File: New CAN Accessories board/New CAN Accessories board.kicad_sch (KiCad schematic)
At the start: 22 parts, among them J10 39301040, J11 ATF13-2P-BM03, J12 Conn_01x02_Pin, J9 39301060, T1 MCP2562FD-E_SN, U1 NUCLEO_L432KC

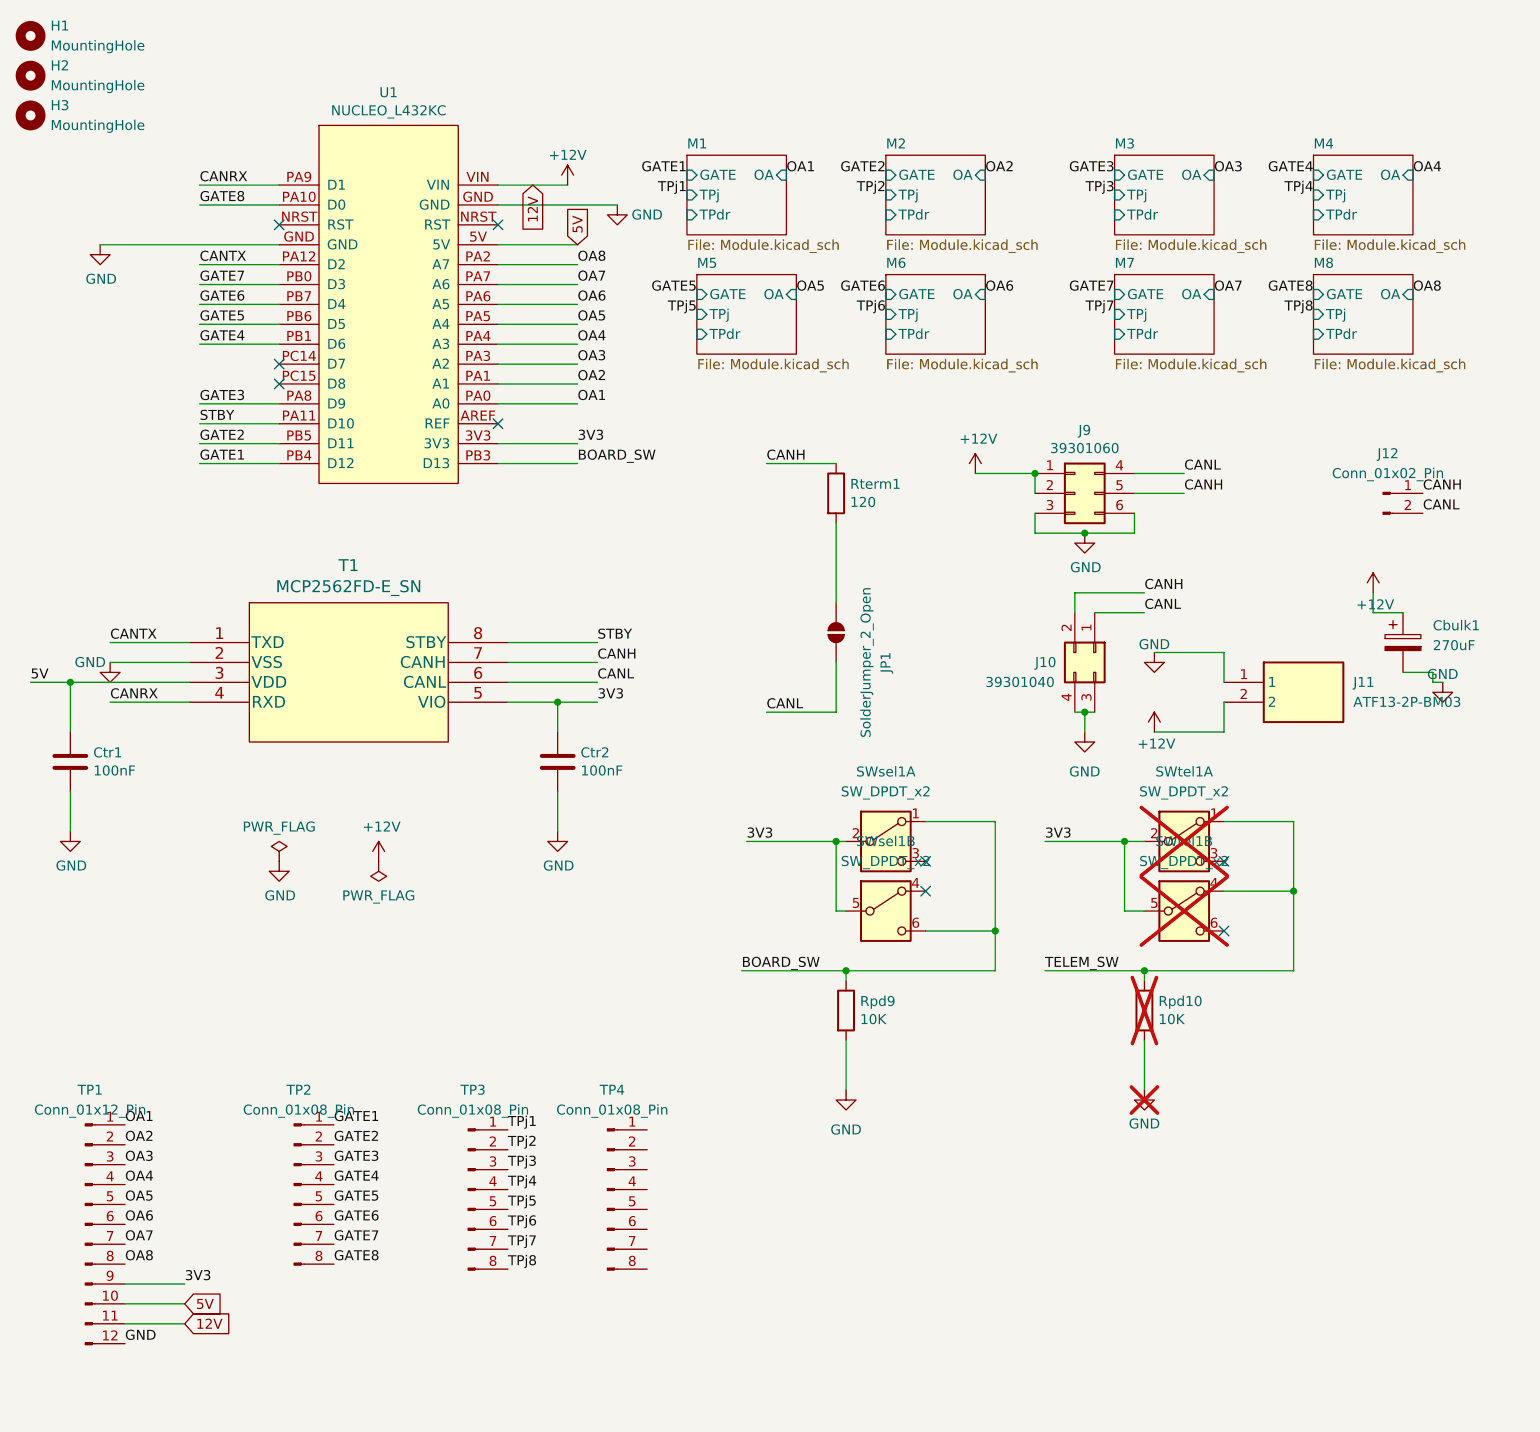
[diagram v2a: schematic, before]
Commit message: 1x16 header test points
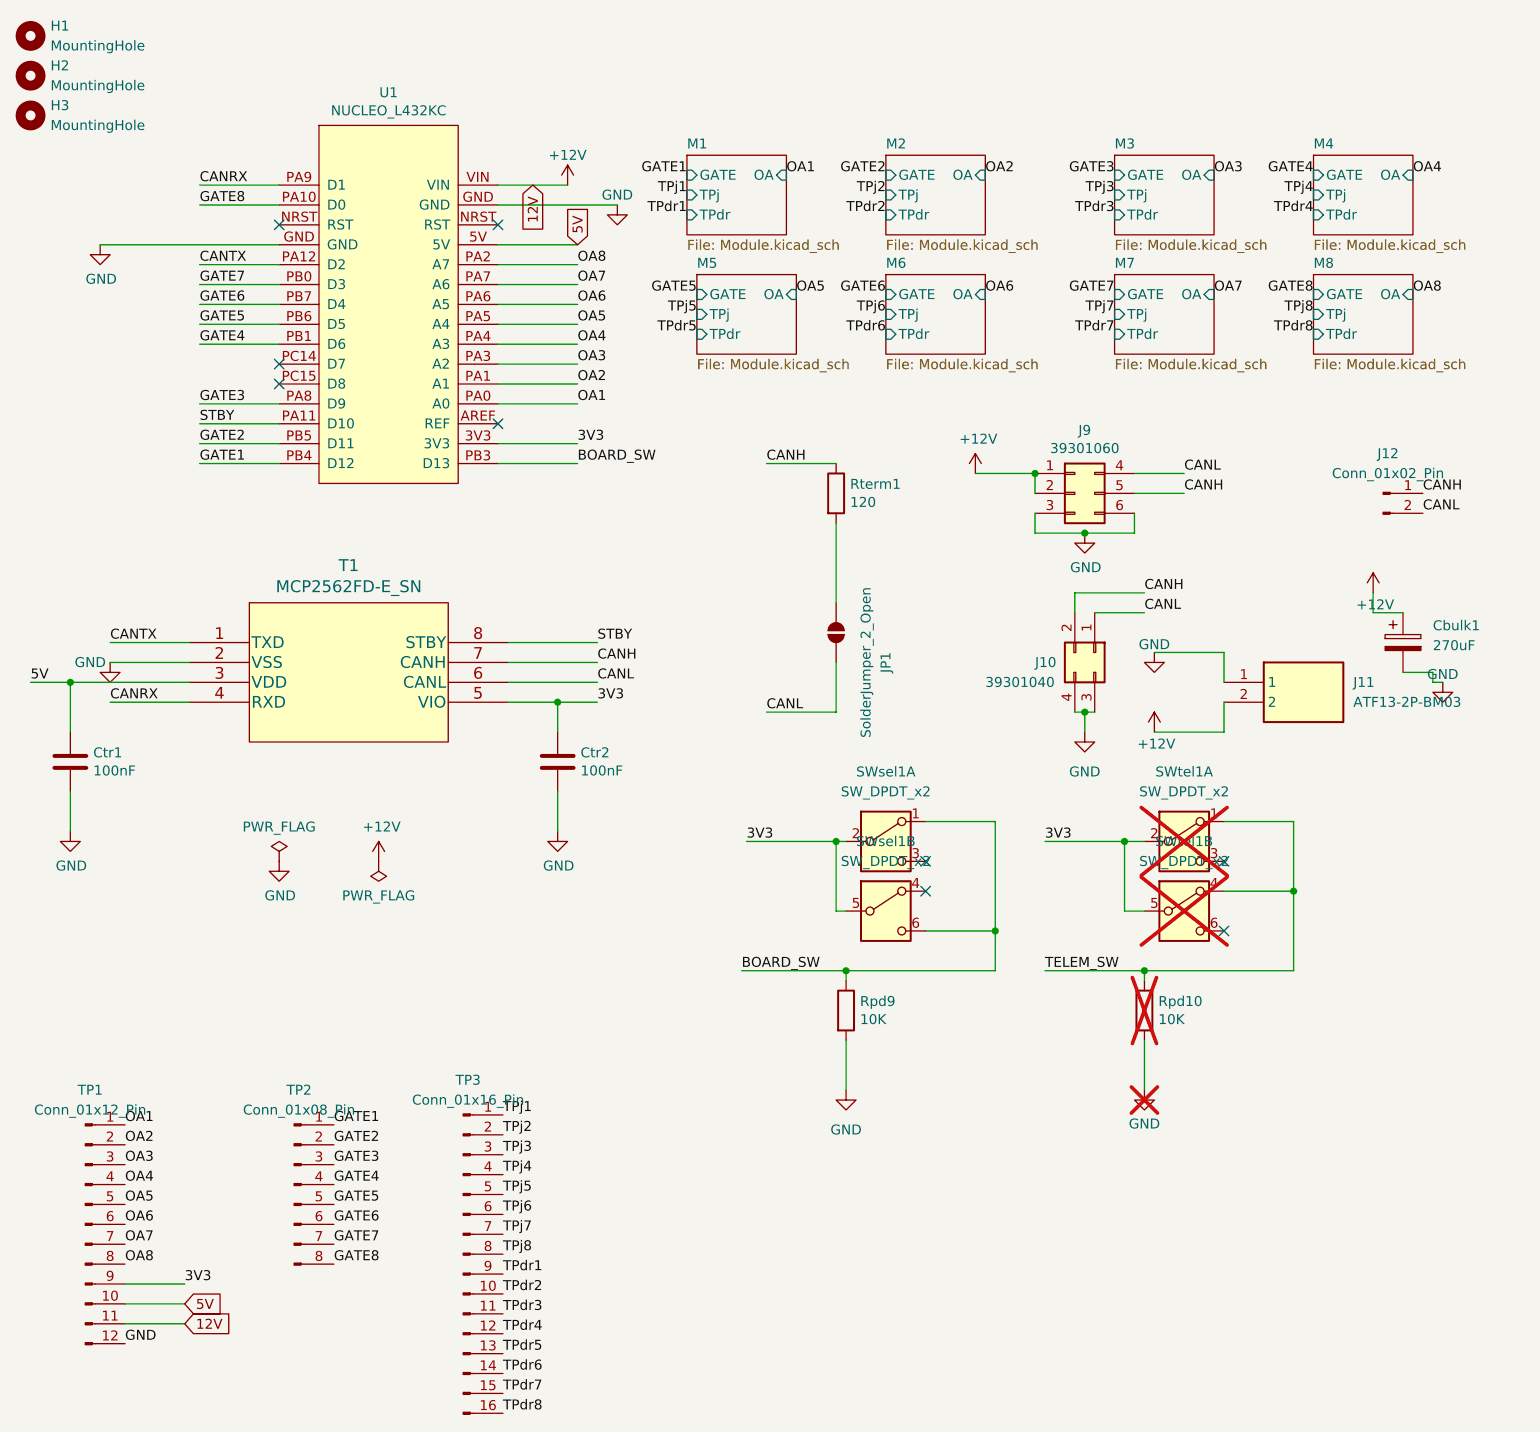
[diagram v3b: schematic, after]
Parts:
- removed TP3, TP4: Conn_01x08_Pin, Connector_PinHeader_2.54mm:PinHeader_1x08_P2.54mm_Vertical, symbol Connector:Conn_01x08_Pin
- added TP3: Conn_01x16_Pin, Connector_PinHeader_2.54mm:PinHeader_1x16_P2.54mm_Vertical, symbol Connector:Conn_01x16_Pin
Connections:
- net TPj1: now also TP3.1 (Pin_1)
- net TPj2: now also TP3.2 (Pin_2)
- net TPj3: now also TP3.3 (Pin_3)
- net TPj4: now also TP3.4 (Pin_4)
- net TPj5: now also TP3.5 (Pin_5)
- net TPj6: now also TP3.6 (Pin_6)
- net TPj7: now also TP3.7 (Pin_7)
- net TPj8: now also TP3.8 (Pin_8)
- new net TPdr1: TP3.9 (Pin_9)
- new net TPdr2: TP3.10 (Pin_10)
- new net TPdr3: TP3.11 (Pin_11)
- new net TPdr4: TP3.12 (Pin_12)
- new net TPdr5: TP3.13 (Pin_13)
- new net TPdr6: TP3.14 (Pin_14)
- new net TPdr7: TP3.15 (Pin_15)
- new net TPdr8: TP3.16 (Pin_16)

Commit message: finalized PCB design
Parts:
- removed J12: Conn_01x02_Pin, Connector_PinHeader_2.54mm:PinHeader_1x02_P2.54mm_Vertical, symbol Connector:Conn_01x02_Pin
- added J12: Conn_01x03_Pin, Connector_PinHeader_2.54mm:PinHeader_1x03_P2.54mm_Vertical, symbol Connector:Conn_01x03_Pin
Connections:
- net CANH: now also J12.1 (Pin_1)
- net CANL: now also J12.2 (Pin_2)
- net GND: now also J12.3 (Pin_3)
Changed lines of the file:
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@@
 	(wire
 		(pts
+			(xy 203.2 85.09) (xy 207.01 85.09)
+		)
+		(stroke
+			(width 0)
+			(type default)
+		)
+	)
+	(wire
+		(pts
 			(xy 186.69 130.81) (xy 186.69 140.97)
 		)
@@
 	)
 	(symbol
+		(lib_id "Connector:Conn_01x03_Pin")
+		(at 198.12 82.55 0)
+		(unit 1)
+		(exclude_from_sim no)
+		(in_bom yes)
+		(on_board yes)
+		(dnp no)
+		(fields_autoplaced yes)
+		(property "Reference" "J12"
+			(at 198.755 74.93 0)
+			(effects
+				(font
+					(size 1.27 1.27)
+				)
+			)
+		)
+		(property "Value" "Conn_01x03_Pin"
+			(at 198.755 77.47 0)
+			(effects
+				(font
+					(size 1.27 1.27)
+				)
+			)
+		)
+		(property "Footprint" "Connector_PinHeader_2.54mm:PinHeader_1x03_P2.54mm_Vertical"
+			(at 198.12 82.55 0)
+			(effects
+				(font
+					(size 1.27 1.27)
+				)
+				(hide yes)
+			)
+		)
+		(property "Datasheet" "~"
+			(at 198.12 82.55 0)
+			(effects
+				(font
+					(size 1.27 1.27)
+				)
+				(hide yes)
+			)
+		)
+		(property "Description" "Generic connector, single row, 01x03, script generated"
+			(at 198.12 82.55 0)
+			(effects
+				(font
+					(size 1.27 1.27)
+				)
+				(hide yes)
+			)
+		)
+		(pin "2"
+		)
+		(pin "3"
+		)
+		(pin "1"
+		)
+		(instances
+			(project ""
+				(path "/88340f43-3f46-45a6-9393-130e00dc3071"
+					(reference "J12")
+					(unit 1)
+				)
+			)
+		)
+	)
+	(symbol
 		(lib_id "Switch:SW_DPDT_x2")
 		(at 134.62 133.35 0)
@@
 	)
 	(symbol
+		(lib_id "power:GND")
+		(at 207.01 85.09 0)
+		(unit 1)
+		(exclude_from_sim no)
+		(in_bom yes)
+		(on_board yes)
+		(dnp no)
+		(fields_autoplaced yes)
+		(property "Reference" "#PWR039"
+			(at 207.01 91.44 0)
+			(effects
+				(font
+					(size 1.27 1.27)
+				)
+				(hide yes)
+			)
+		)
+		(property "Value" "GND"
+			(at 207.01 90.17 0)
+			(effects
+				(font
+					(size 1.27 1.27)
+				)
+			)
+		)
+		(property "Footprint" ""
+			(at 207.01 85.09 0)
+			(effects
+				(font
+					(size 1.27 1.27)
+				)
+				(hide yes)
+			)
+		)
+		(property "Datasheet" ""
+			(at 207.01 85.09 0)
+			(effects
+				(font
+					(size 1.27 1.27)
+				)
+				(hide yes)
+			)
+		)
+		(property "Description" "Power symbol creates a global label with name \"GND\" , ground"
+			(at 207.01 85.09 0)
+			(effects
+				(font
+					(size 1.27 1.27)
+				)
+				(hide yes)
+			)
+		)
+		(pin "1"
+		)
+		(instances
+			(project ""
+				(path "/88340f43-3f46-45a6-9393-130e00dc3071"
+					(reference "#PWR039")
+					(unit 1)
+				)
+			)
+		)
+	)
+	(symbol
 		(lib_id "Switch:SW_DPDT_x2")
 		(at 172.72 133.35 0)
@@
 					(unit 1)
 				)
-			)
-		)
-	)
-	(symbol
-		(lib_id "Connector:Conn_01x02_Pin")
-		(at 198.12 80.01 0)
-		(unit 1)
-		(exclude_from_sim no)
-		(in_bom yes)
-		(on_board yes)
-		(dnp no)
-		(fields_autoplaced yes)
-		(property "Reference" "J12"
-			(at 198.755 74.93 0)
-			(effects
-				(font
-					(size 1.27 1.27)
-				)
-			)
-		)
-		(property "Value" "Conn_01x02_Pin"
-			(at 198.755 77.47 0)
-			(effects
-				(font
-					(size 1.27 1.27)
-				)
-			)
-		)
-		(property "Footprint" "Connector_PinHeader_2.54mm:PinHeader_1x02_P2.54mm_Vertical"
-			(at 198.12 80.01 0)
-			(effects
-				(font
-					(size 1.27 1.27)
-				)
-				(hide yes)
-			)
-		)
-		(property "Datasheet" "~"
-			(at 198.12 80.01 0)
-			(effects
-				(font
-					(size 1.27 1.27)
-				)
-				(hide yes)
-			)
-		)
-		(property "Description" "Generic connector, single row, 01x02, script generated"
-			(at 198.12 80.01 0)
-			(effects
-				(font
-					(size 1.27 1.27)
-				)
-				(hide yes)
-			)
-		)
-		(pin "1"
-		)
-		(pin "2"
-		)
-		(instances
-			(project ""
-				(path "/88340f43-3f46-45a6-9393-130e00dc3071"
-					(reference "J12")
-					(unit 1)
-				)
